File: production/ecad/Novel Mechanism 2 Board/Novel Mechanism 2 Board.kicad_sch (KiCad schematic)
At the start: 15 parts, among them J1 1755736, J2 1755736, J3 Conn_01x10_Pin, SW1 SW_DPDT_x2, U1 L9958SBTR

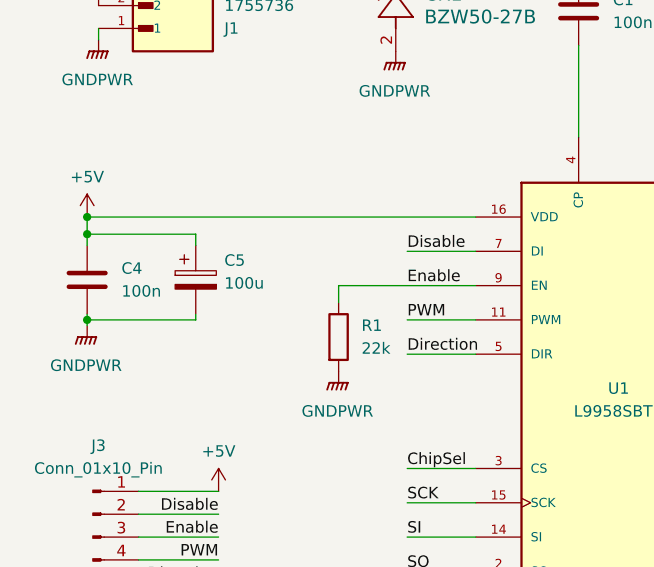
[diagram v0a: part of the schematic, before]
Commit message: added electrolytic caps
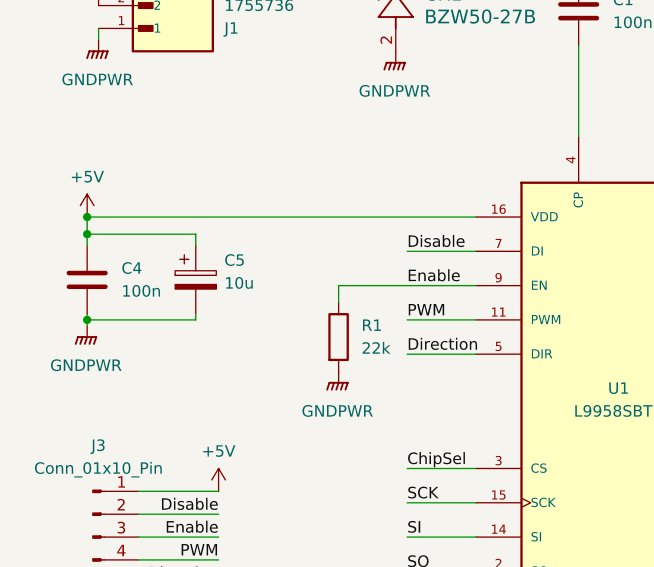
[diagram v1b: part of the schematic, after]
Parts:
- C2: footprint (none) -> Capacitor_SMD:EDK107M063A9PAA
- C5: value 100u -> 10u; footprint (none) -> Capacitor_SMD:EDK106M050A9GAA
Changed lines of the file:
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@@
       (effects (font (size 1.27 1.27)) (justify left))
     )
-    (property "Value" "100u" (at 38.735 67.056 0)
-      (effects (font (size 1.27 1.27)) (justify left))
-    )
-    (property "Footprint" "" (at 36.5252 70.485 0)
+    (property "Value" "10u" (at 38.735 67.056 0)
+      (effects (font (size 1.27 1.27)) (justify left))
+    )
+    (property "Footprint" "Capacitor_SMD:EDK106M050A9GAA" (at 36.5252 70.485 0)
       (effects (font (size 1.27 1.27)) hide)
     )
@@
       (effects (font (size 1.27 1.27)) (justify left))
     )
-    (property "Footprint" "" (at 94.9452 40.64 0)
-      (effects (font (size 1.27 1.27)) hide)
-    )
+    (property "Footprint" "Capacitor_SMD:EDK107M063A9PAA" (at 94.9452 40.64 0)
+      (effects (font (size 1.27 1.27)) hide)
+    )

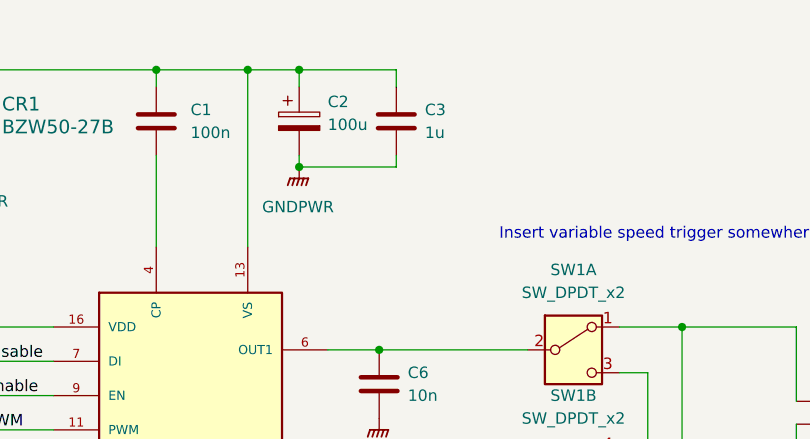
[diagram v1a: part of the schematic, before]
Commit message: added capacitor and resistor footprints
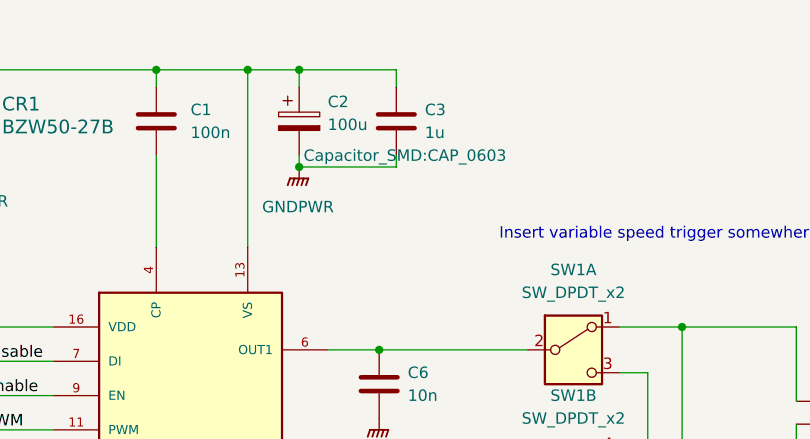
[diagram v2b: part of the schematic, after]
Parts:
- C1, C3, C4, C6, C7: footprint (none) -> Capacitor_SMD:CAP_0603
- R1, R2: footprint (none) -> Resistor_SMD:RES_0603
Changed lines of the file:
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@@
       (effects (font (size 1.27 1.27)) (justify left))
     )
-    (property "Footprint" "" (at 103.8352 83.82 0)
+    (property "Footprint" "Capacitor_SMD:CAP_0603" (at 103.8352 83.82 0)
       (effects (font (size 1.27 1.27)) hide)
     )
@@
       (effects (font (size 1.27 1.27)) (justify left))
     )
-    (property "Footprint" "" (at 79.0702 40.64 0)
+    (property "Footprint" "Capacitor_SMD:CAP_0603" (at 79.0702 40.64 0)
       (effects (font (size 1.27 1.27)) hide)
     )
@@
       (effects (font (size 1.27 1.27)) (justify left))
     )
-    (property "Footprint" "" (at 103.8352 69.85 0)
+    (property "Footprint" "Capacitor_SMD:CAP_0603" (at 103.8352 69.85 0)
       (effects (font (size 1.27 1.27)) hide)
     )
@@
       (effects (font (size 1.27 1.27)) (justify left))
     )
-    (property "Footprint" "" (at 57.277 106.68 90)
+    (property "Footprint" "Resistor_SMD:RES_0603" (at 57.277 106.68 90)
       (effects (font (size 1.27 1.27)) hide)
     )
@@
       (effects (font (size 1.27 1.27)) (justify left))
     )
-    (property "Footprint" "" (at 24.4602 70.485 0)
+    (property "Footprint" "Capacitor_SMD:CAP_0603" (at 24.4602 70.485 0)
       (effects (font (size 1.27 1.27)) hide)
     )
@@
       (effects (font (size 1.27 1.27)) (justify left))
     )
-    (property "Footprint" "" (at 105.7402 40.64 0)
-      (effects (font (size 1.27 1.27)) hide)
+    (property "Footprint" "Capacitor_SMD:CAP_0603" (at 105.7402 40.64 0)
+      (effects (font (size 1.27 1.27)))
     )
     (property "Datasheet" "~" (at 104.775 36.83 0)
@@
       (effects (font (size 1.27 1.27)) (justify left))
     )
-    (property "Footprint" "" (at 49.657 73.025 90)
-      (effects (font (size 1.27 1.27)) hide)
-    )
+    (property "Footprint" "Resistor_SMD:RES_0603" (at 49.657 73.025 90)
+      (effects (font (size 1.27 1.27)) hide)
+    )

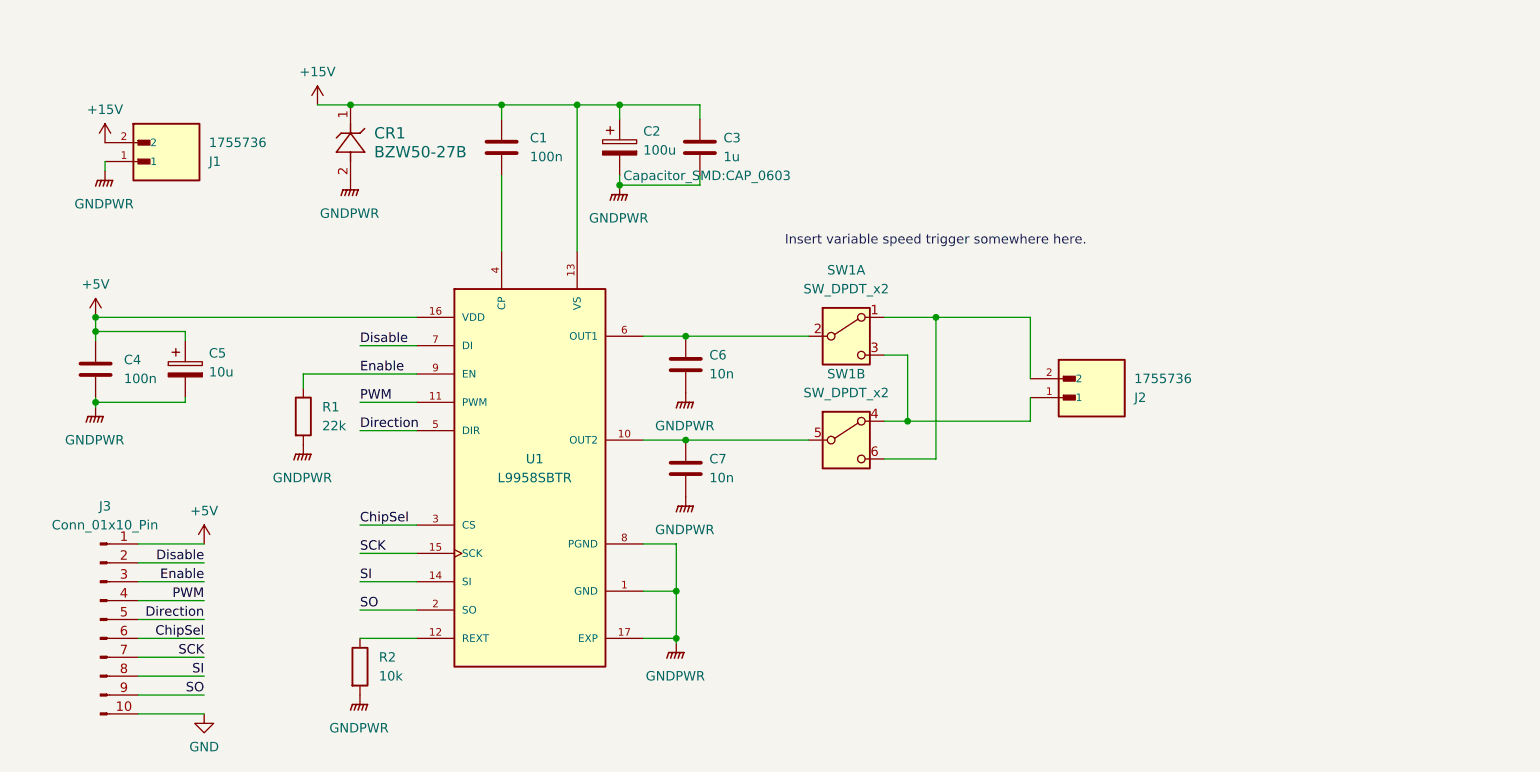
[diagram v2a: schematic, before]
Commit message: fixed erc errors
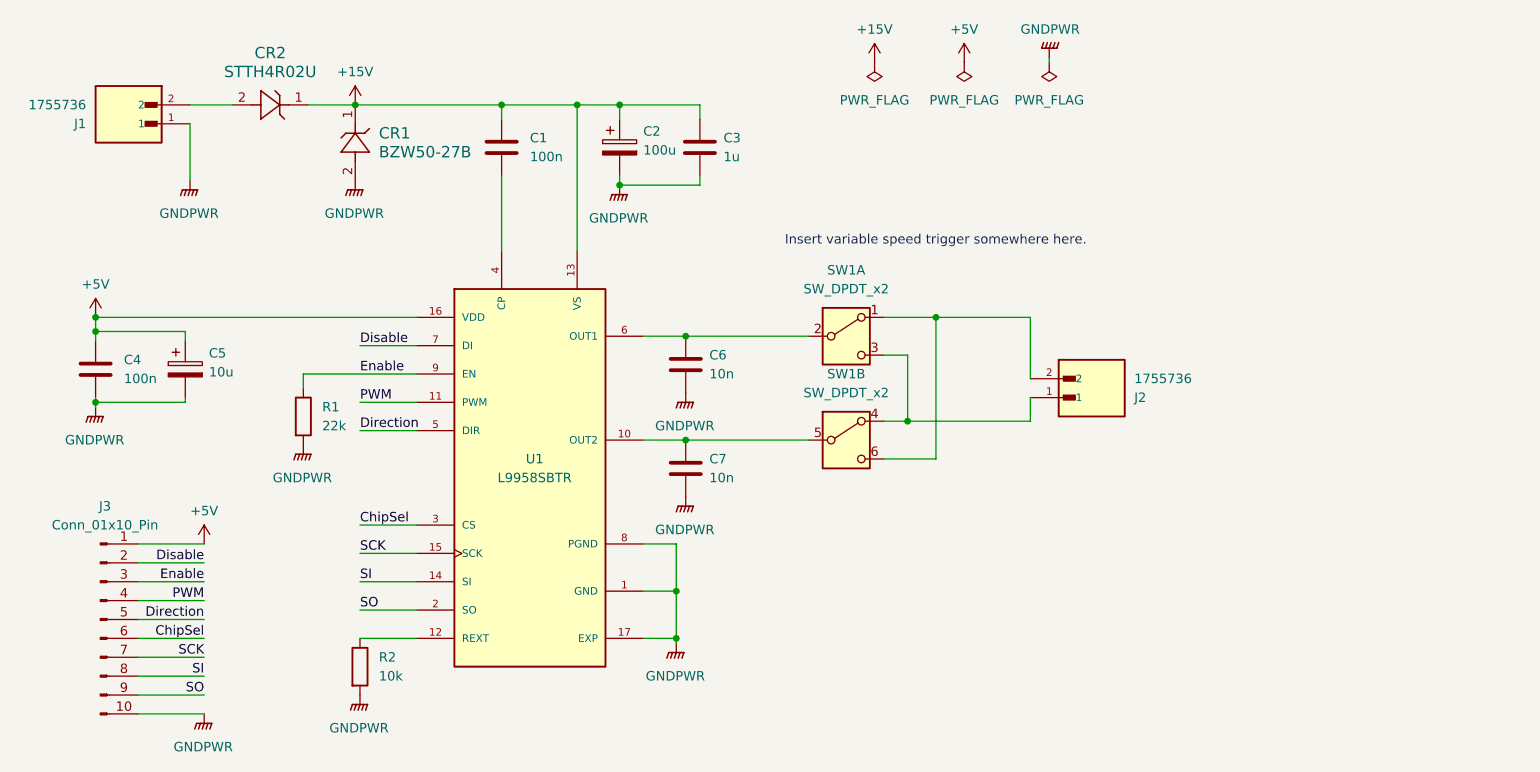
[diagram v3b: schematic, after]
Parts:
- added CR2: STTH4R02U, Diode_SMD:STTH4R02U, symbol BZW50-27B:BZW50-27B
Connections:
- net GND is gone; now on net GNDPWR: J3.10 (Pin_10)
- net +15V: now also CR2.1; no longer J1.2
- new net: CR2.2, J1.2
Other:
- moved on the sheet: CR1, J1

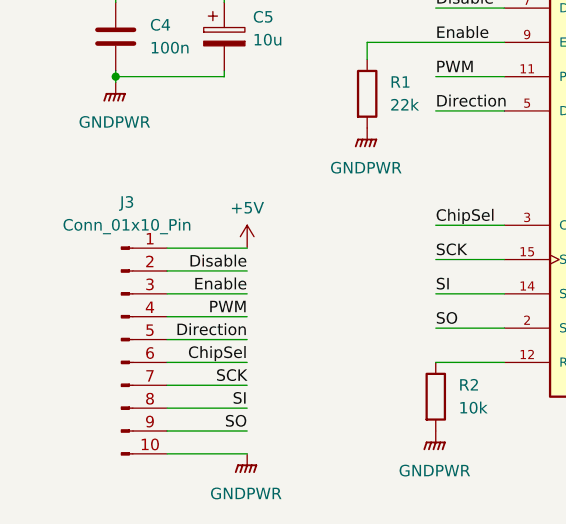
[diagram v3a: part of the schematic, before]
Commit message: changed 10 to 12 pin connector
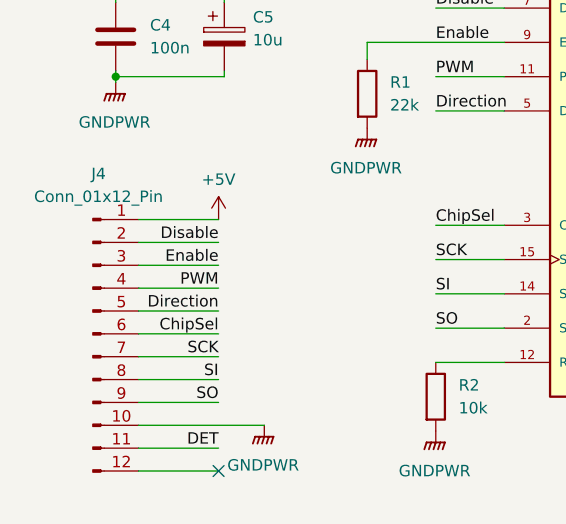
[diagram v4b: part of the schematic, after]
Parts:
- removed J3: Conn_01x10_Pin, symbol Connector:Conn_01x10_Pin
- added J4: Conn_01x12_Pin, symbol Connector:Conn_01x12_Pin
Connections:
- net +5V: now also J4.1 (Pin_1)
- net ChipSel: now also J4.6 (Pin_6)
- net Direction: now also J4.5 (Pin_5)
- net Disable: now also J4.2 (Pin_2)
- net Enable: now also J4.3 (Pin_3)
- net GNDPWR: now also J4.10 (Pin_10)
- net PWM: now also J4.4 (Pin_4)
- net SCK: now also J4.7 (Pin_7)
- net SI: now also J4.8 (Pin_8)
- net SO: now also J4.9 (Pin_9)
- new net DET: J4.11 (Pin_11)
- no-connect marks 0 -> 1

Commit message: schematic fixes
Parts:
- removed SW1: SW_DPDT_x2, symbol Switch:SW_DPDT_x2
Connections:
- net at C7.1, U1.10 (OUT2): now also J2.1
- net at C6.1, U1.6 (OUT1): now also J2.2
- net GNDPWR renamed GND
- net GND: no longer C2.2, C3.2
- new net: C2.2, C3.2
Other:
- moved on the sheet: J2

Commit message: preliminary component placement
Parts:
- CR1: footprint R6_STM -> Diode_THT:BZW50-27B
- J1, J2: footprint 1755736:PHOENIX_1755736 -> Connector:PHOENIX_1755736
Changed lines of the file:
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@@
       (effects (font (size 1.27 1.27)) (justify left))
     )
-    (property "Footprint" "1755736:PHOENIX_1755736" (at 28.575 33.655 0)
+    (property "Footprint" "Connector:PHOENIX_1755736" (at 28.575 33.655 0)
       (effects (font (size 1.27 1.27)) (justify bottom) hide)
     )
@@
       (effects (font (size 1.524 1.524)) (justify left))
     )
-    (property "Footprint" "R6_STM" (at 58.42 31.115 0)
+    (property "Footprint" "Diode_THT:BZW50-27B" (at 58.42 31.115 0)
       (effects (font (size 1.27 1.27) italic) hide)
     )
@@
       (effects (font (size 1.27 1.27)) (justify left))
     )
-    (property "Footprint" "1755736:PHOENIX_1755736" (at 127 70.485 0)
-      (effects (font (size 1.27 1.27)) (justify bottom) hide)
-    )
+    (property "Footprint" "Connector:PHOENIX_1755736" (at 127 70.485 0)
+      (effects (font (size 1.27 1.27)) (justify bottom) hide)
+    )

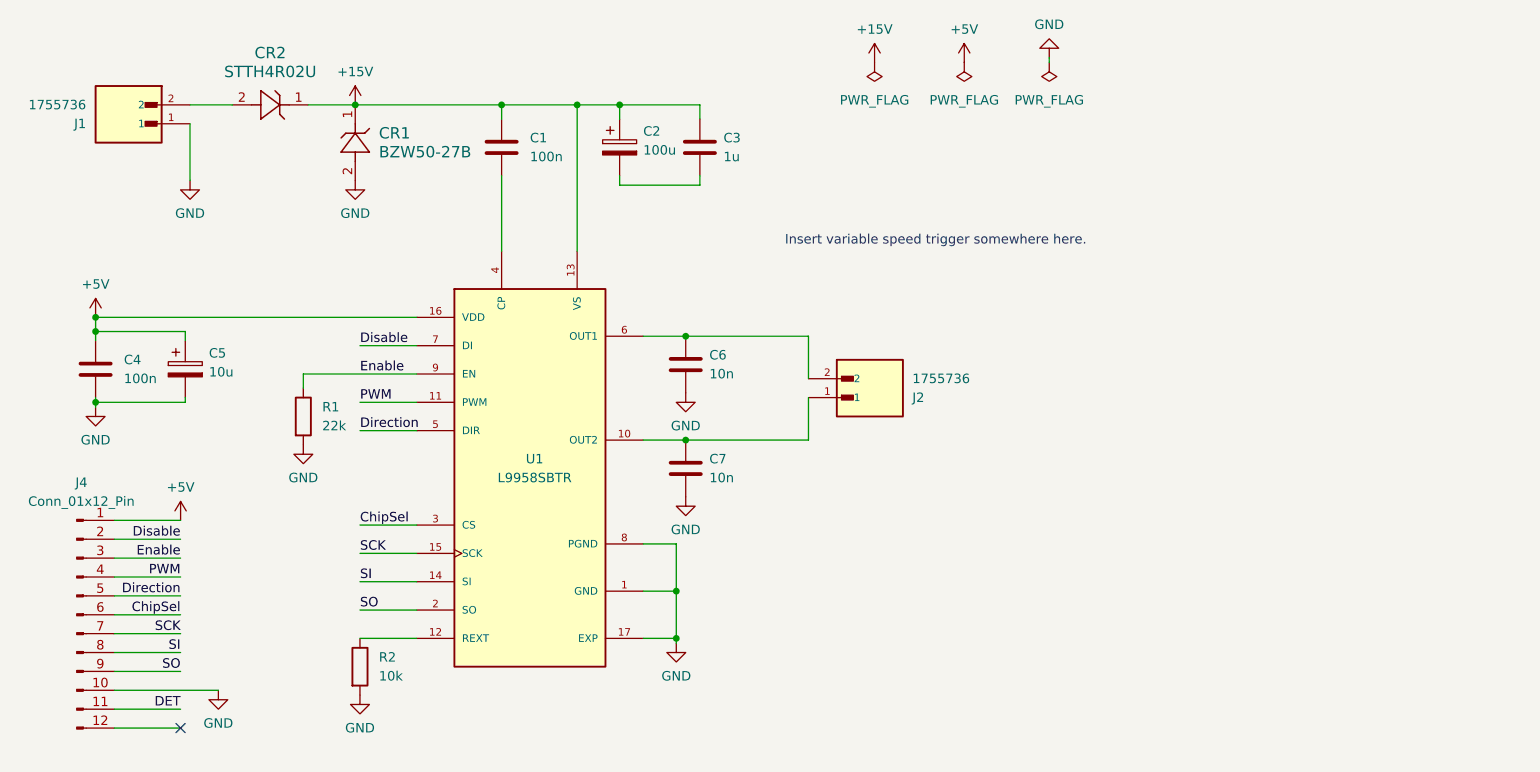
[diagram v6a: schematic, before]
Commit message: added hall effect current sense for adc output to microcontroller
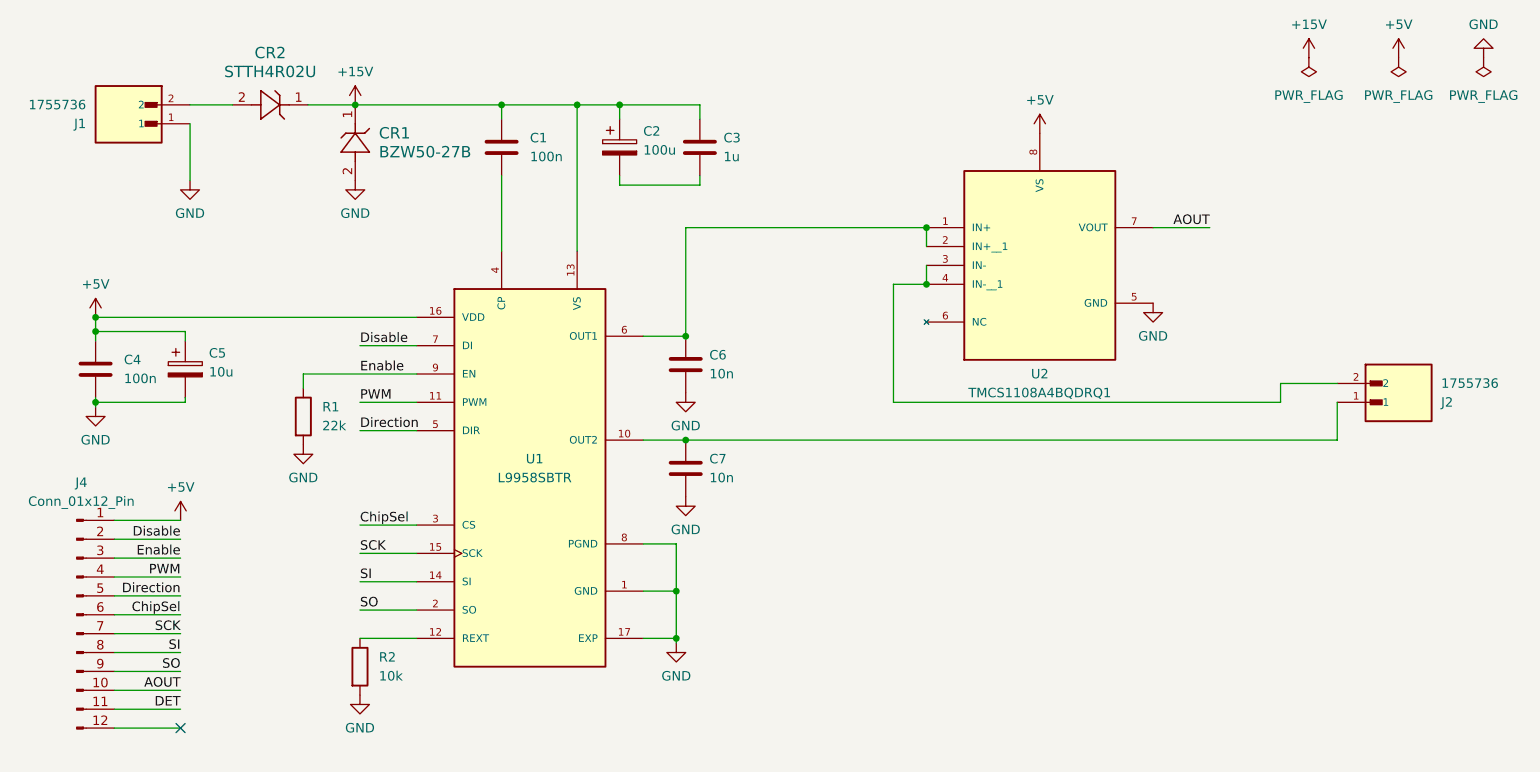
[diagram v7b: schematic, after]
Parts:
- added U2: TMCS1108A4BQDRQ1, TMCS1108A4BQDRQ1:SOIC127P599X175-8N, symbol Interface_CAN_LIN:TMCS1108A4BQDRQ1
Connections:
- net +5V: now also U2.8 (VS)
- net GND: now also U2.5 (GND); no longer J4.10 (Pin_10)
- net at C6.1, U1.6 (OUT1): now also U2.1 (IN+), U2.2 (IN+__1); no longer J2.2
- new net: J2.2, U2.3 (IN-), U2.4 (IN-__1)
- new net AOUT: J4.10 (Pin_10), U2.7 (VOUT)
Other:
- note removed: "Insert variable speed trigger somewhere here."
- moved on the sheet: J2

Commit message: added component to layout
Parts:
- U2: footprint TMCS1108A4BQDRQ1:SOIC127P599X175-8N -> Package_SO:TMCS1108A4BQDRQ1
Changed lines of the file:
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@@
       (effects (font (size 1.27 1.27)))
     )
-    (property "Footprint" "TMCS1108A4BQDRQ1:SOIC127P599X175-8N" (at 150.495 50.165 0)
+    (property "Footprint" "Package_SO:TMCS1108A4BQDRQ1" (at 150.495 50.165 0)
       (effects (font (size 1.27 1.27)) (justify bottom) hide)
     )
